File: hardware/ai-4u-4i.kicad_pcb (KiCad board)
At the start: 4 copper layers, 100 x 85 mm, 131 parts, among them J101 TNG-Power-TOP, J102 TNG-Power-BTM, J103 TNG-Data-TOP, J104 TNG-Data-BTM, P102 Debug, P103 PE, P201 INPUT0, P202 INPUT1, P203 INPUT2, P204 INPUT3, Q101 FDS8449, SW101 BOOT, T101 744273222, U101 STM32F070CBT6, U102 AZ1117EH, U103 82400152, U104 TEL10, U105 TLP293, U106 STEF01, U201 ISO1212, U202 ISO1212, U203 ISO1212, U204 ISO1212, X101 TBD

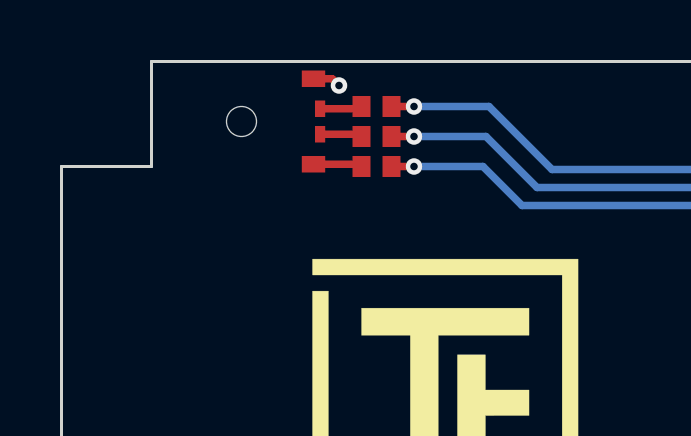
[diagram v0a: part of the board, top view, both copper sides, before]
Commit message: increase rgb led diameter
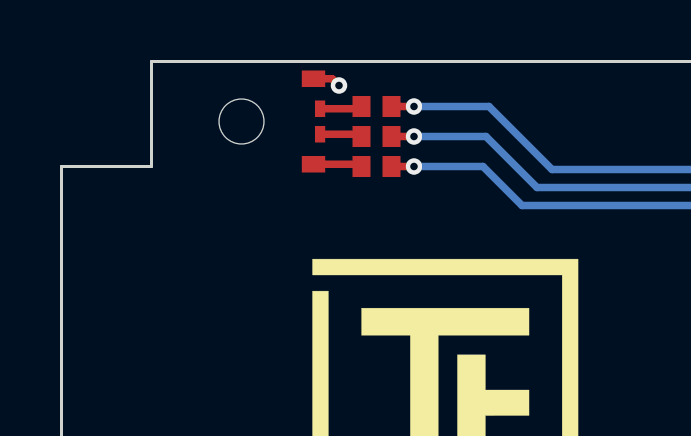
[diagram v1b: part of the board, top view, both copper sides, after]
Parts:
- LED101: footprint LED-RGB-LP -> kicad-libraries:LED-RGB-LP
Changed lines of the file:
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@@
     (add_net USB-DPC)
   )
+  (module kicad-libraries:LED-RGB-LP (layer F.Cu)
+    (at 98.2 64.5 90)
+    (fp_text reference LED101 (at 0 0 90) (layer F.Fab)
+      (effects (font (size 0.15 0.15) (thickness 0.0375)))
+    )
+    (fp_text value EASV3015RGBA0 (at 0 -0.3 90) (layer F.Fab)
+      (effects (font (size 0.15 0.15) (thickness 0.0375)))
+    )
+    (fp_line (start -1 -1.4) (end 1 -1.4) (layer F.Fab) (width 0.1))
+    (fp_line (start 1 -1.4) (end 1 -8.4) (layer F.Fab) (width 0.1))
+    (fp_line (start 1 -8.4) (end -1 -8.4) (layer F.Fab) (width 0.1))
+    (fp_line (start -1 -8.4) (end -1 -1.4) (layer F.Fab) (width 0.1))
+    (fp_line (start -1.5 -0.5) (end -1.5 0.2) (layer F.Fab) (width 0.025))
+    (fp_line (start 1.5 -0.5) (end -1.5 -0.5) (layer F.Fab) (width 0.025))
+    (fp_line (start 1.5 0.2) (end 1.5 -0.5) (layer F.Fab) (width 0.025))
+    (fp_line (start -1.5 0.2) (end 1.5 0.2) (layer F.Fab) (width 0.025))
+    (fp_arc (start 0 -0.5) (end -0.8 -0.5) (angle 90) (layer F.Fab) (width 0.025))
+    (fp_arc (start 0 -0.5) (end 0 -1.3) (angle 90) (layer F.Fab) (width 0.025))
+    (pad 3 smd rect (at -0.425 0.22 90) (size 0.55 0.34) (layers F.Cu F.Paste F.Mask)
+      (net 49 "Net-(LED101-Pad3)"))
+    (pad 2 smd rect (at 0.425 0.22 90) (size 0.55 0.34) (layers F.Cu F.Paste F.Mask)
+      (net 48 "Net-(LED101-Pad2)"))
+    (pad 4 smd rect (at -1.425 0 90) (size 0.55 0.78) (layers F.Cu F.Paste F.Mask)
+      (net 47 "Net-(LED101-Pad4)"))
+    (pad 1 smd rect (at 1.425 0 90) (size 0.55 0.78) (layers F.Cu F.Paste F.Mask)
+      (net 2 3V3))
+    (pad "" np_thru_hole circle (at 0 -2.4 90) (size 1.5 1.5) (drill 1.5) (layers *.Cu *.Mask))
+    (model ${KICAD_SYMBOL_DIR}/3d/LED_SMD/LED_RGB_LP.wrl
+      (at (xyz 0 0 0))
+      (scale (xyz 1 1 1))
+      (rotate (xyz 0 0 0))
+    )
+  )
   (module kicad-libraries:Fiducial_Mark (layer B.Cu)
     (at 99.8 145.5)
@@
     )
   )
-  (module LED-RGB-LP (layer F.Cu)
-    (at 98.2 64.5 90)
-    (fp_text reference LED101 (at 0 0 90) (layer F.Fab)
-      (effects (font (size 0.15 0.15) (thickness 0.0375)))
-    )
-    (fp_text value EASV3015RGBA0 (at 0 -0.3 90) (layer F.Fab)
-      (effects (font (size 0.15 0.15) (thickness 0.0375)))
-    )
-    (fp_arc (start 0 -0.5) (end 0 -1.3) (angle 90) (layer F.Fab) (width 0.025))
-    (fp_arc (start 0 -0.5) (end -0.8 -0.5) (angle 90) (layer F.Fab) (width 0.025))
-    (fp_line (start -1.5 0.2) (end 1.5 0.2) (layer F.Fab) (width 0.025))
-    (fp_line (start 1.5 0.2) (end 1.5 -0.5) (layer F.Fab) (width 0.025))
-    (fp_line (start 1.5 -0.5) (end -1.5 -0.5) (layer F.Fab) (width 0.025))
-    (fp_line (start -1.5 -0.5) (end -1.5 0.2) (layer F.Fab) (width 0.025))
-    (fp_line (start -1 -8.4) (end -1 -1.4) (layer F.Fab) (width 0.1))
-    (fp_line (start 1 -8.4) (end -1 -8.4) (layer F.Fab) (width 0.1))
-    (fp_line (start 1 -1.4) (end 1 -8.4) (layer F.Fab) (width 0.1))
-    (fp_line (start -1 -1.4) (end 1 -1.4) (layer F.Fab) (width 0.1))
-    (pad "" np_thru_hole circle (at 0 -2.4 90) (size 1 1) (drill 1) (layers *.Cu *.Mask))
-    (pad 1 smd rect (at 1.425 0 90) (size 0.55 0.78) (layers F.Cu F.Paste F.Mask)
-      (net 2 3V3))
-    (pad 4 smd rect (at -1.425 0 90) (size 0.55 0.78) (layers F.Cu F.Paste F.Mask)
-      (net 47 "Net-(LED101-Pad4)"))
-    (pad 2 smd rect (at 0.425 0.22 90) (size 0.55 0.34) (layers F.Cu F.Paste F.Mask)
-      (net 48 "Net-(LED101-Pad2)"))
-    (pad 3 smd rect (at -0.425 0.22 90) (size 0.55 0.34) (layers F.Cu F.Paste F.Mask)
-      (net 49 "Net-(LED101-Pad3)"))
-  )
   (module kicad-libraries:Logo_TF_10x12 (layer F.Cu)

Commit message: schematic finished
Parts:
- added REF**: SMB, kicad-libraries:SMB, F.Cu at (116.4, 113.4)
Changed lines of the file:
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@@
     (tracks 1555)
     (zones 0)
-    (modules 131)
+    (modules 132)
     (nets 107)
   )
@@
     (add_net USB-DPC)
   )
+  (module kicad-libraries:SMB (layer F.Cu)
+    (at 116.4 113.4 90)
+    (fp_text reference REF** (at 0 0.5 90) (layer F.SilkS)
+      (effects (font (size 0.15 0.15) (thickness 0.0375)))
+    )
+    (fp_text value SMB (at 0 -0.5 90) (layer F.Fab)
+      (effects (font (size 0.15 0.15) (thickness 0.0375)))
+    )
+    (fp_line (start -2.3 2) (end -2.3 -2) (layer F.SilkS) (width 0.15))
+    (fp_line (start 2.3 2) (end -2.3 2) (layer F.SilkS) (width 0.15))
+    (fp_line (start 2.3 -2) (end 2.3 2) (layer F.SilkS) (width 0.15))
+    (fp_line (start -2.3 -2) (end 2.3 -2) (layer F.SilkS) (width 0.15))
+    (fp_line (start 1 2) (end 1 -2) (layer F.SilkS) (width 0.15))
+    (fp_line (start 1.2 -2) (end 1.2 2) (layer F.SilkS) (width 0.15))
+    (fp_line (start 1.1 -2) (end 1.1 1.9) (layer F.SilkS) (width 0.15))
+    (fp_line (start 1.3 -2) (end 1.3 2) (layer F.SilkS) (width 0.15))
+    (fp_line (start 1.4 -2) (end 1.4 2) (layer F.SilkS) (width 0.15))
+    (pad 2 smd rect (at 2.11 0 90) (size 1.62 2.18) (layers F.Cu F.Paste F.Mask))
+    (pad 1 smd rect (at -2.11 0 90) (size 1.62 2.18) (layers F.Cu F.Paste F.Mask))
+  )
   (module kicad-libraries:LED-RGB-LP (layer F.Cu)

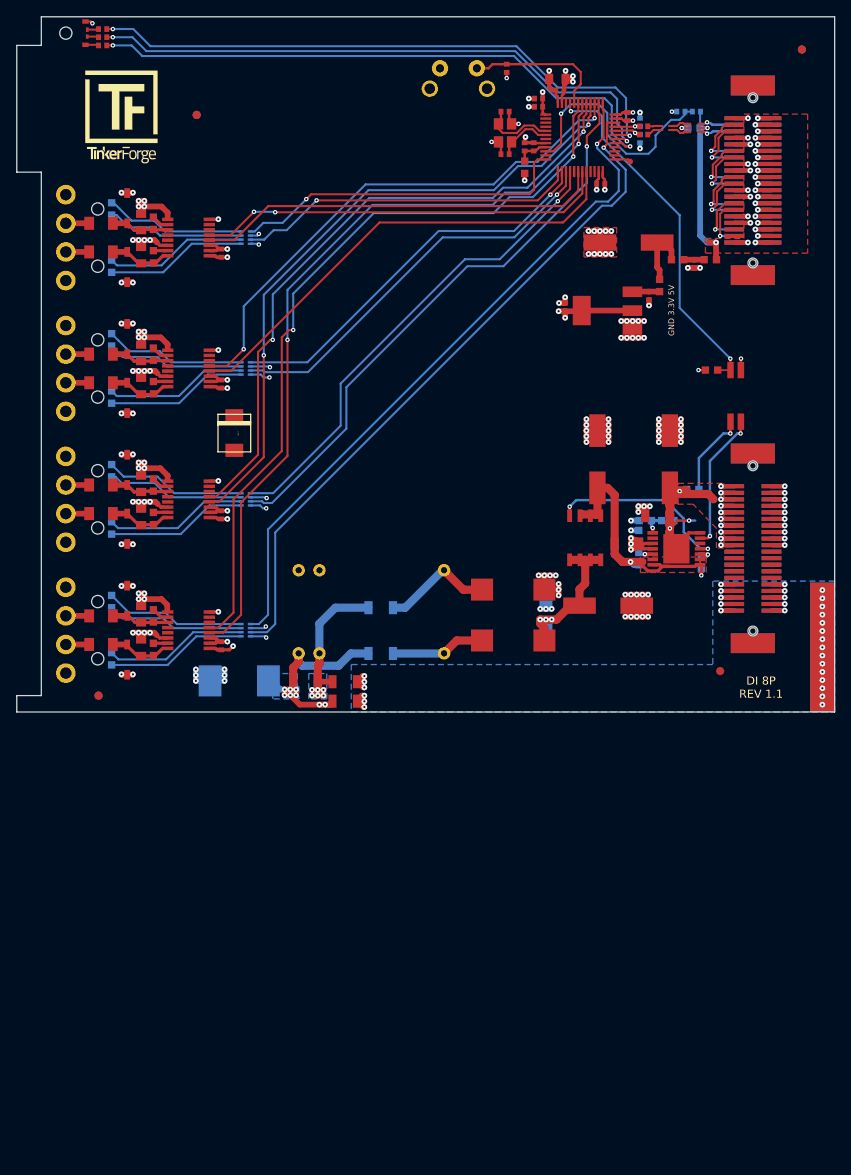
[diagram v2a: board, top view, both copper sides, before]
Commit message: fix inductor footprint
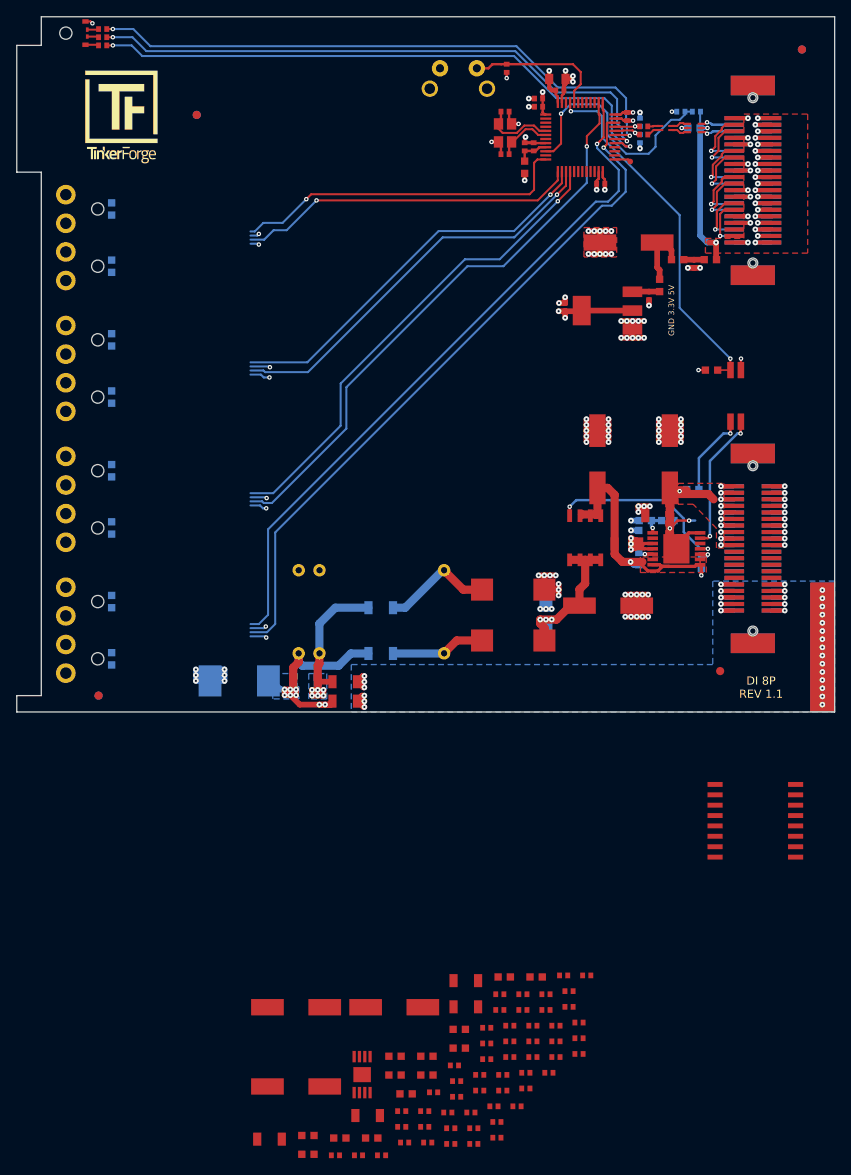
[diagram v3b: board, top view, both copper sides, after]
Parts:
- removed C202, C203, C205, C206, C207, C208, C209, C210: DNP, C0805
- removed C204, C211, C212, C213: 100nF, C0402F
- removed D201, D202, D211, D212, D213, D214, D215, D216: SMF36CA, SOD-123
- removed R201, R202, R205, R206, R207, R208, R209, R210: 1k, RMELF
- removed R203, R204, R211, R212, R213, R214, R215, R216: 562, R0603F
- removed REF**: SMB, kicad-libraries:SMB
- removed RP201, RP202, RP203, RP204: 470, kicad-libraries:4X0402
- removed U201, U202, U204: ISO1212, SSOP16
- added C201: 27nF, kicad-libraries:C1206, F.Cu at (144.7, 183.6)
- added C214: 2700pF, kicad-libraries:C0603F, F.Cu at (129.3, 199.6)
- added C215: 2700pF, kicad-libraries:C0603F, F.Cu at (140.0, 189.6)
- added C216: 2700pF, kicad-libraries:C0603F, F.Cu at (143.9, 186.3)
- added C217: 10nF, kicad-libraries:C0402F, F.Cu at (156.7, 179.7)
- added C218: 10nF, kicad-libraries:C0402F, F.Cu at (136.9, 198.2)
- added C219: 10nF, kicad-libraries:C0402F, F.Cu at (151.7, 183.9)
- added C220: 10nF, kicad-libraries:C0402F, F.Cu at (147.3, 188.0)
- added C221: 10nF, kicad-libraries:C0402F, F.Cu at (143.3, 190.7)
- added C222: 10nF, kicad-libraries:C0402F, F.Cu at (154.5, 183.9)
- added C223: 10nF, kicad-libraries:C0402F, F.Cu at (140.8, 194.0)
- added C224: 10nF, kicad-libraries:C0402F, F.Cu at (136.9, 196.3)
- added C226: 1uF, kicad-libraries:C0402F, F.Cu at (131.6, 201.7)
- added C227: 1uF, kicad-libraries:C0402F, F.Cu at (128.8, 201.7)
- added C228: 1uF, kicad-libraries:C0402F, F.Cu at (149.2, 193.8)
- added C229: 1uF, kicad-libraries:C0402F, F.Cu at (148.5, 199.6)
- added C230: 10µF, kicad-libraries:C1206, F.Cu at (120.7, 199.7)
- added C231: 10µF, kicad-libraries:C1206, F.Cu at (144.7, 180.4)
- added C232: 22uF, kicad-libraries:C1206, F.Cu at (132.7, 196.8)
- added C233: 100nF, kicad-libraries:C0402F, F.Cu at (151.7, 182.0)
- added C234: 100µF/35V, kicad-libraries:ELKO_83, F.Cu at (124.0, 183.6)
- added C235: 100nF, kicad-libraries:C0402F, F.Cu at (148.9, 182.0)
- added C236: 1uF, kicad-libraries:C0402F, F.Cu at (147.3, 186.1)
- added C237: 1uF, kicad-libraries:C0402F, F.Cu at (148.9, 183.9)
- added C238: 10nF, kicad-libraries:C0402F, F.Cu at (139.7, 196.3)
- added C239: 10nF, kicad-libraries:C0402F, F.Cu at (134.4, 201.7)
- added C240: 1uF, kicad-libraries:C0402F, F.Cu at (150.1, 185.9)
- added C241: 1uF, kicad-libraries:C0402F, F.Cu at (154.5, 182.0)
- added C242: 1uF, kicad-libraries:C0402F, F.Cu at (143.6, 192.6)
- added C243: 1uF, kicad-libraries:C0402F, F.Cu at (147.3, 190.0)
- added C244: 100nF, kicad-libraries:C0402F, F.Cu at (150.1, 187.8)
- added C245: 100nF, kicad-libraries:C0402F, F.Cu at (139.7, 198.2)
- added C246: TBD, kicad-libraries:ELKO_83, F.Cu at (136.0, 183.6)
- added C247: TBD, kicad-libraries:ELKO_83, F.Cu at (124.0, 193.3)
- added L201: FB, kicad-libraries:C0603F, F.Cu at (136.1, 189.6)
- added L202: FB, kicad-libraries:C0603F, F.Cu at (149.4, 179.9)
- added R217: 1k, kicad-libraries:R0603F, F.Cu at (136.1, 191.9)
- added R218: 1k, kicad-libraries:R0603F, F.Cu at (125.4, 201.6)
- added R219: 1k, kicad-libraries:R0603F, F.Cu at (137.4, 194.2)
- added R220: 1k, kicad-libraries:R0603F, F.Cu at (125.4, 199.3)
- added R221: 1k, kicad-libraries:R0603F, F.Cu at (153.3, 179.9)
- added R222: 1k, kicad-libraries:R0603F, F.Cu at (143.9, 188.6)
- added R223: 1k, kicad-libraries:R0603F, F.Cu at (140.0, 191.9)
- added R224: 1k, kicad-libraries:R0603F, F.Cu at (133.2, 199.6)
- added R225: 10M, kicad-libraries:R0402F, F.Cu at (137.2, 200.1)
- added R226: 10M, kicad-libraries:R0402F, F.Cu at (157.3, 181.6)
- added R227: 10M, kicad-libraries:R0402F, F.Cu at (150.1, 189.7)
- added R228: 10M, kicad-libraries:R0402F, F.Cu at (158.5, 189.3)
- added R229: 10M, kicad-libraries:R0402F, F.Cu at (140.0, 200.1)
- added R230: 10M, kicad-libraries:R0402F, F.Cu at (143.6, 194.6)
- added R231: 10M, kicad-libraries:R0402F, F.Cu at (142.5, 196.5)
- added R232: 10M, kicad-libraries:R0402F, F.Cu at (157.3, 183.6)
- added R233: 0, kicad-libraries:R0402F, F.Cu at (149.2, 191.9)
- added R234: 1.1k, kicad-libraries:R0402F, F.Cu at (145.3, 196.5)
- added R235: 0, kicad-libraries:R0402F, F.Cu at (155.7, 185.9)
- added R236: 1.1k, kicad-libraries:R0402F, F.Cu at (152.9, 189.7)
- added R237: 0, kicad-libraries:R0402F, F.Cu at (155.7, 187.8)
- added R238: 1.1k, kicad-libraries:R0402F, F.Cu at (152.9, 187.8)
- added R239: 0, kicad-libraries:R0402F, F.Cu at (148.5, 197.6)
- added R240: 1.1k, kicad-libraries:R0402F, F.Cu at (151.0, 195.7)
- added R241: 0, kicad-libraries:R0402F, F.Cu at (154.9, 191.6)
- added R242: 1.1k, kicad-libraries:R0402F, F.Cu at (152.0, 193.5)
- added R243: 0, kicad-libraries:R0402F, F.Cu at (145.7, 200.3)
- added R244: 1.1k, kicad-libraries:R0402F, F.Cu at (158.5, 187.4)
- added R245: 0, kicad-libraries:R0402F, F.Cu at (155.7, 189.7)
- added R246: 1.1k, kicad-libraries:R0402F, F.Cu at (158.5, 185.5)
- added R247: 0, kicad-libraries:R0402F, F.Cu at (152.9, 185.9)
- added R248: 1.1k, kicad-libraries:R0402F, F.Cu at (145.7, 198.4)
- added R251: 4.7k, kicad-libraries:R0402F, F.Cu at (148.1, 195.7)
- added R252: 4.7k, kicad-libraries:R0402F, F.Cu at (152.0, 191.6)
- added R253: TBD, kicad-libraries:R0402F, F.Cu at (142.9, 200.3)
- added R254: 4.7k, kicad-libraries:R0402F, F.Cu at (142.9, 198.4)
- added R255: 47, kicad-libraries:R0402F, F.Cu at (146.4, 193.8)
- added R256: TBD, kicad-libraries:R0402F, F.Cu at (159.5, 179.7)
- added R257: TBD, kicad-libraries:R0402F, F.Cu at (146.4, 191.9)
- added U205: TPS7A6633QDGNRQ1, kicad-libraries:MSOP-8-EP, F.Cu at (132.0, 191.8)
- LED101: footprint kicad-libraries:LED-RGB-LP -> LED-RGB-LP
- U203: value ISO1212 -> ISO7741DWR; footprint SSOP16 -> kicad-libraries:SOIC16_WIDE
- moved U203 79.7 mm to (180.1, 160.8)
- turned T101 to 180 degrees
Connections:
- T101 pad 1: Net-(C120-Pad2) -> Net-(C121-Pad1)
- T101 pad 3: Net-(C121-Pad1) -> Net-(C120-Pad2)
- U101 pad 17: (no net) -> LED5
- U101 pad 18: IN0 -> (no net)
- U101 pad 19: IN1 -> (no net)
- U101 pad 20: IN2 -> (no net)
- U101 pad 38: LED5 -> SPI-CS
- U101 pad 39: IN3 -> SPI-CLK
- U101 pad 40: IN4 -> SPI-MISO
- U101 pad 41: IN5 -> SPI-MOSI
- U101 pad 42: IN6 -> ADC-RESET
- U101 pad 43: IN7 -> (no net)
- U203 pad 1: GND -> 3V3
- U203 pad 12: (no net) -> Net-(U201-Pad38)
- U203 pad 13: (no net) -> Net-(U201-Pad37)
- U203 pad 14: AGND -> Net-(U201-Pad1)
- U203 pad 15: Net-(R213-Pad1) -> AGND
- U203 pad 16: Net-(C207-Pad2) -> DVDD
- U203 pad 2: 3V3 -> GND
- U203 pad 3: 3V3 -> SPI-MOSI
- U203 pad 4: IN4 -> SPI-CLK
- U203 pad 5: IN5 -> SPI-CS
- U203 pad 6: (no net) -> Net-(R255-Pad2)
- U203 pad 7: (no net) -> Net-(R254-Pad2)
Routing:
- net IN6: track 95.1 -> 0.00 mm, vias 2 -> 0
- net IN7: track 94.1 -> 0.00 mm, vias 2 -> 0
- net AGND: track 123.3 -> 33.0 mm, vias 60 -> 12
- net IN4: track 79.9 -> 0.00 mm, vias 2 -> 0
- net IN5: track 78.6 -> 0.00 mm, vias 2 -> 0
- net SPI-CS: track 0.00 -> 70.9 mm, vias 0 -> 1
- net LED5: track 70.9 -> 0.00 mm, vias 1 -> 0
- net IN3: track 64.7 -> 0.00 mm, vias 2 -> 0
- net IN2: track 58.2 -> 0.00 mm
- net IN1: track 50.4 -> 0.00 mm, vias 2 -> 0
- net IN0: track 49.9 -> 0.00 mm
- net Net-(D210-Pad2): track 17.5 -> 0.00 mm
- net Net-(D208-Pad2): track 17.5 -> 0.00 mm
- net Net-(D204-Pad2): track 17.4 -> 0.00 mm
- net Net-(D206-Pad2): track 17.4 -> 0.00 mm
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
